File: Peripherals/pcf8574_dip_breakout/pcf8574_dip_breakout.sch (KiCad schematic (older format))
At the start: 24 parts, among them J1 I2C, J2 IO, U1 PCF8574

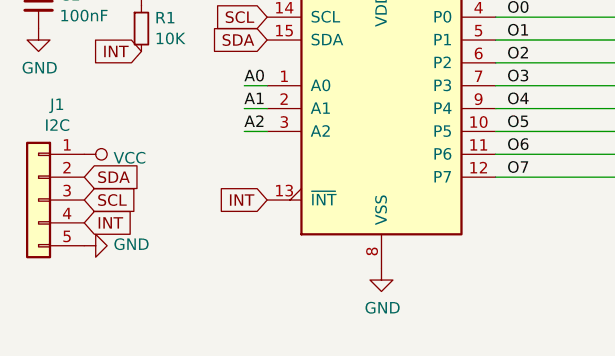
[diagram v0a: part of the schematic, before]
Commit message: PCF8574 breakout: did not close KiCad before commit, fixing
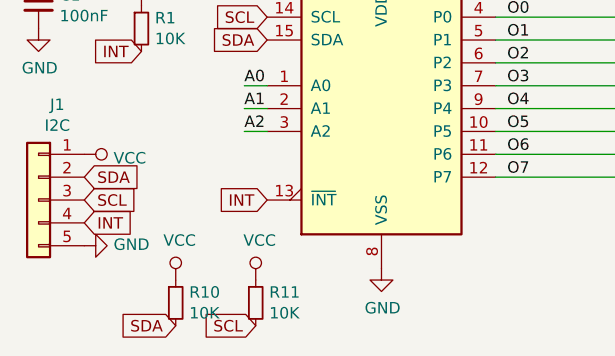
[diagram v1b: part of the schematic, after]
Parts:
- added R10, R11: 10K, pcf8574_dip_breakout:R_0805_10K_HandSoldering, symbol Device:R_Small
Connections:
- net SCL: now also R11.2
- net SDA: now also R10.2
- net VCC: now also R10.1, R11.1
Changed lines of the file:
@@
 	1    0    0    -1
 $EndComp
+$Comp
+L Device:R_Small R10
+U 1 1 5DCEF607
+P 4100 3750
+F 0 "R10" H 4159 3796 50  0000 L CNN
+F 1 "10K" H 4159 3705 50  0000 L CNN
+F 2 "pcf8574_dip_breakout:R_0805_10K_HandSoldering" H 4100 3750 50  0001 C CNN
+F 3 "~" H 4100 3750 50  0001 C CNN
+	1    4100 3750
+	1    0    0    -1
+$EndComp
+$Comp
+L power:VCC #PWR0124
+U 1 1 5DCEF60F
+P 4100 3650
+F 0 "#PWR0124" H 4100 3500 50  0001 C CNN
+F 1 "VCC" H 4117 3823 50  0000 C CNN
+F 2 "" H 4100 3650 50  0001 C CNN
+F 3 "" H 4100 3650 50  0001 C CNN
+	1    4100 3650
+	1    0    0    -1
+$EndComp
+$Comp
+L Device:R_Small R11
+U 1 1 5DCEFBDA
+P 4450 3750
+F 0 "R11" H 4509 3796 50  0000 L CNN
+F 1 "10K" H 4509 3705 50  0000 L CNN
+F 2 "pcf8574_dip_breakout:R_0805_10K_HandSoldering" H 4450 3750 50  0001 C CNN
+F 3 "~" H 4450 3750 50  0001 C CNN
+	1    4450 3750
+	1    0    0    -1
+$EndComp
+$Comp
+L power:VCC #PWR0125
+U 1 1 5DCEFBE2
+P 4450 3650
+F 0 "#PWR0125" H 4450 3500 50  0001 C CNN
+F 1 "VCC" H 4467 3823 50  0000 C CNN
+F 2 "" H 4450 3650 50  0001 C CNN
+F 3 "" H 4450 3650 50  0001 C CNN
+	1    4450 3650
+	1    0    0    -1
+$EndComp
+Text GLabel 4100 3850 0    50   Input ~ 0
+SDA
+Text GLabel 4450 3850 0    50   Input ~ 0
+SCL
 $EndSCHEMATC
